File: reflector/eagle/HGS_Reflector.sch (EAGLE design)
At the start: 22 parts, among them J1 U.FL, U1 TQP3M9037, U2 TQP3M903X, U3 LP2985XX-N

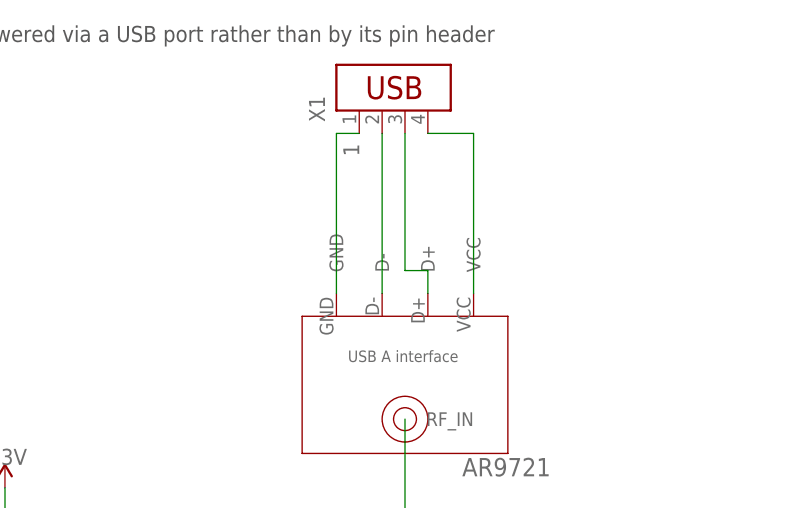
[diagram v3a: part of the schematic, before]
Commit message: Fixed USB pin issue
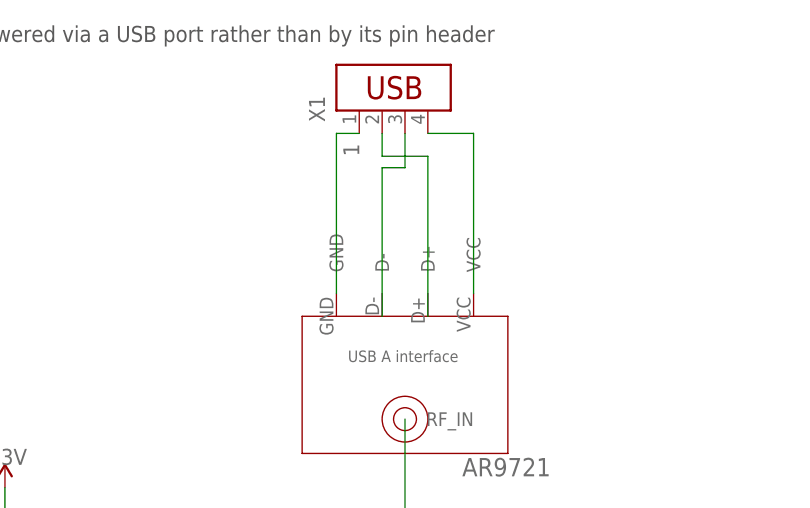
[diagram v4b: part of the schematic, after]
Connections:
- removed net N$16: X1.3
- new net N$6: U$4.D+, X1.2
- net N$14: now also U$4.D-, X1.3; no longer X1.2
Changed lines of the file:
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@@
+</segment>
+</net>
+<net name="N$6" class="0">
+<segment>
+<pinref part="X1" gate="G$1" pin="2"/>
+<wire x1="255.27" y1="189.23" x2="255.27" y2="186.69" width="0.1524" layer="91"/>
+<wire x1="255.27" y1="186.69" x2="260.35" y2="186.69" width="0.1524" layer="91"/>
+<pinref part="U$4" gate="G$1" pin="D+"/>
+<wire x1="260.35" y1="186.69" x2="260.35" y2="168.91" width="0.1524" layer="91"/>
 </segment>
 </net>
 <net name="N$14" class="0">
 <segment>
-<pinref part="X1" gate="G$1" pin="2"/>
-<wire x1="255.27" y1="189.23" x2="255.27" y2="171.45" width="0.1524" layer="91"/>
+<pinref part="U$4" gate="G$1" pin="D-"/>
+<wire x1="255.27" y1="168.91" x2="255.27" y2="185.42" width="0.1524" layer="91"/>
+<wire x1="255.27" y1="185.42" x2="257.81" y2="185.42" width="0.1524" layer="91"/>
+<pinref part="X1" gate="G$1" pin="3"/>
+<wire x1="257.81" y1="185.42" x2="257.81" y2="189.23" width="0.1524" layer="91"/>
 </segment>
 </net>
-<net name="N$16" class="0">
-<segment>
-<pinref part="X1" gate="G$1" pin="3"/>
-<wire x1="257.81" y1="189.23" x2="257.81" y2="173.99" width="0.1524" layer="91"/>
-<wire x1="257.81" y1="173.99" x2="260.35" y2="173.99" width="0.1524" layer="91"/>
-<wire x1="260.35" y1="173.99" x2="260.35" y2="171.45" width="0.1524" layer="91"/>
-</segment>
-</net>

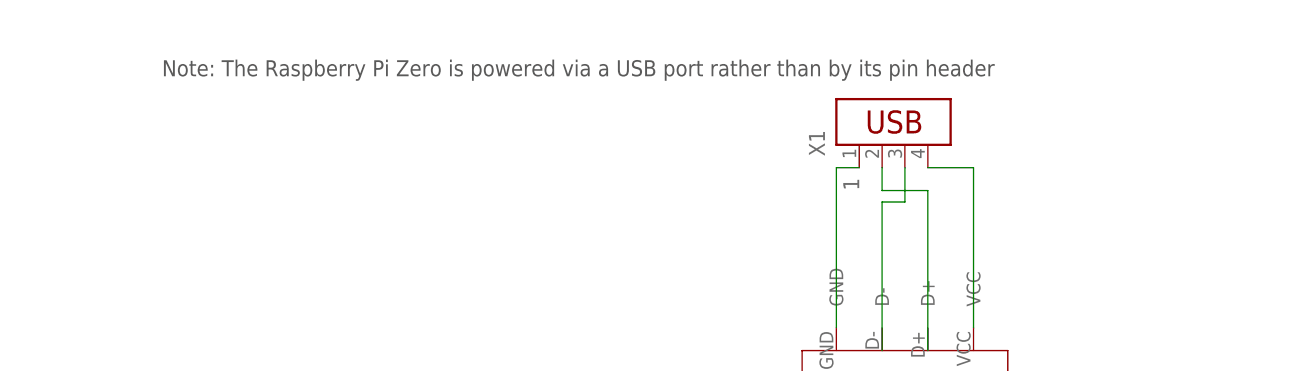
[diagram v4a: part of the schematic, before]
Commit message: Fixed USB A port name
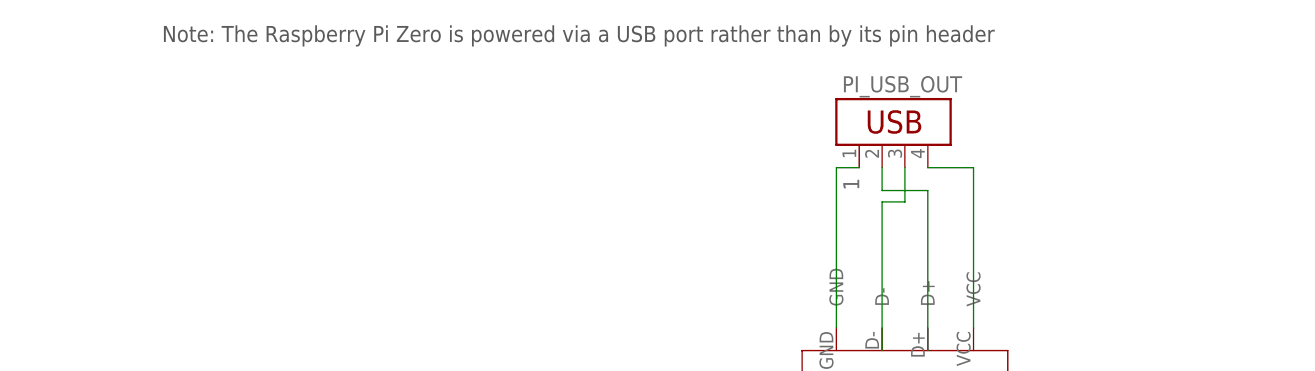
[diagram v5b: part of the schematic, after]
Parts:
- renumbered X1 to PI_USB_OUT
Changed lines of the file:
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@@
 <part name="U$3" library="HGS_Data_Parts" deviceset="1/4_WAVE_TRF" device=""/>
 <part name="ANT1" library="discrete" library_urn="urn:adsk.eagle:library:211" deviceset="ANTENNA" device="" package3d_urn="urn:adsk.eagle:package:12928/1"/>
-<part name="X1" library="con-amp" library_urn="urn:adsk.eagle:library:127" deviceset="USB-787616" device="" package3d_urn="urn:adsk.eagle:package:8081650/1"/>
+<part name="PI_USB_OUT" library="con-amp" library_urn="urn:adsk.eagle:library:127" deviceset="USB-787616" device="" package3d_urn="urn:adsk.eagle:package:8081650/1"/>
 <part name="LED1" library="eagle-ltspice" library_urn="urn:adsk.eagle:library:217" deviceset="LED_E" device="" package3d_urn="urn:adsk.eagle:package:13319/2"/>
 <part name="GND10" library="supply1" library_urn="urn:adsk.eagle:library:371" deviceset="GND" device=""/>
@@
 <text x="180.34" y="27.94" size="3.048" layer="94">OreSat Live Handheld Ground Station Reflector</text>
 <text x="265.43" y="6.35" size="3.048" layer="94">2</text>
-<text x="175.26" y="199.39" size="1.778" layer="97">Note: The Raspberry Pi Zero is powered via a USB port rather than by its pin header</text>
+<text x="175.26" y="203.2" size="1.778" layer="97">Note: The Raspberry Pi Zero is powered via a USB port rather than by its pin header</text>
 <text x="274.32" y="90.17" size="1.778" layer="97" rot="R180">Note: J1 connects to the Atheros WiFi Adapter via coax</text>
 </plain>
@@
 <attribute name="VALUE" x="49.53" y="113.03" size="1.778" layer="96"/>
 </instance>
-<instance part="X1" gate="G$1" x="257.81" y="194.31" smashed="yes" rot="R90">
-<attribute name="NAME" x="248.92" y="190.5" size="1.778" layer="95" rot="R90"/>
+<instance part="PI_USB_OUT" gate="G$1" x="257.81" y="194.31" smashed="yes" rot="R90">
+<attribute name="NAME" x="264.16" y="199.39" size="1.778" layer="95" rot="R180"/>
 <attribute name="VALUE" x="265.43" y="190.5" size="1.778" layer="96" rot="R90"/>
 </instance>
@@
 <net name="1" class="0">
 <segment>
-<pinref part="X1" gate="G$1" pin="1"/>
+<pinref part="PI_USB_OUT" gate="G$1" pin="1"/>
 <label x="252.73" y="186.69" size="1.778" layer="95" rot="R90"/>
 <wire x1="252.73" y1="189.23" x2="250.19" y2="189.23" width="0.1524" layer="91"/>
@@
 <net name="N$15" class="0">
 <segment>
-<pinref part="X1" gate="G$1" pin="4"/>
+<pinref part="PI_USB_OUT" gate="G$1" pin="4"/>
 <wire x1="260.35" y1="189.23" x2="265.43" y2="189.23" width="0.1524" layer="91"/>
 <wire x1="265.43" y1="189.23" x2="265.43" y2="171.45" width="0.1524" layer="91"/>
@@
 <net name="N$6" class="0">
 <segment>
-<pinref part="X1" gate="G$1" pin="2"/>
+<pinref part="PI_USB_OUT" gate="G$1" pin="2"/>
 <wire x1="255.27" y1="189.23" x2="255.27" y2="186.69" width="0.1524" layer="91"/>
 <wire x1="255.27" y1="186.69" x2="260.35" y2="186.69" width="0.1524" layer="91"/>
@@
 <wire x1="255.27" y1="168.91" x2="255.27" y2="185.42" width="0.1524" layer="91"/>
 <wire x1="255.27" y1="185.42" x2="257.81" y2="185.42" width="0.1524" layer="91"/>
-<pinref part="X1" gate="G$1" pin="3"/>
+<pinref part="PI_USB_OUT" gate="G$1" pin="3"/>
 <wire x1="257.81" y1="185.42" x2="257.81" y2="189.23" width="0.1524" layer="91"/>
 </segment>

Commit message: Schematic, board and BOM updates
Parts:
- removed C5, C7: (no value), oresat-rcl:C-EU0402-C-NOSILK
- removed U1: TQP3M9037, U-Qorvo-TQP3M9037-LNA:TQP3M9037
- removed U2: TQP3M903X, U-Qorvo-TQP3M903x-LNA:TQP3M903X
- added C11: 100 pF, oresat-rcl:C-EU0603-C-NOSILK
- added C12: 1 uF, oresat-rcl:C-EU0603-C-NOSILK
- added C14: 100 pF, oresat-rcl:C-EU0402-C-NOSILK
- added L2: (no value), rcl:L-EUL3216C
- added PI_USB_OUT1: (no value), con-amp:USB-787616
- added U$6, U$7: LNA-TP3M9037, HGS_Data_Parts:LNA-TP3M9037
- C1, C6: value (none) -> 100 pF
- C2: value (none) -> 1 uF
- C3, C4: value (none) -> 100 pF; device oresat-rcl:C-EU0603-C-NOSILK -> oresat-rcl:C-EU0402-C-NOSILK
- C8: value 0.1 uF -> 10 nF
- C9: value 0.1 uF -> 2.2 uF
- L1: SPICEPREFIX (none) -> 20 nH
- R9: value (none) -> 2K
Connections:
- removed net N$13: C9.1, U3.VOUT
- removed net N$14: PI_USB_OUT.3, U$4.D-
- removed net N$15: PI_USB_OUT.4
- removed net N$7: C5.1, U$1.RF-OUT
- new net N$16: C14.1, L2.1, U$7.OUT
- new net N$18: PI_USB_OUT.2, PI_USB_OUT1.2, U$4.D+
- new net N$19: PI_USB_OUT.3, PI_USB_OUT1.3, U$4.D-
- new net VCC: PI_USB_OUT.4, PI_USB_OUT1.4, U$4.VCC
- net 1: now also PI_USB_OUT1.1, U$4.GND
- net 3.3V: now also C11.1, C12.1, C9.1, L2.2, U3.VOUT; no longer C3.1, C4.1
- net GND: now also C11.2, C12.2, U$6.GND, U$6.SHTDN, U$7.GND, U$7.SHTDN; no longer C3.2, C4.2, U$3.GND_1, U1.GND, U1.SHTDN, U2.GND, U2.SHTDN
- net N$11: now also U$7.IN; no longer U2.IN
- net N$2: now also C4.1, L1.1, U$6.OUT; no longer J1.SIGNAL, U$2.RF-OUT, U$4.RF_IN
- net N$3: now also C4.2; no longer C7.2, U$2.RF_IN
- net N$4: now also C3.1, U$1.RF-OUT; no longer C5.2, U1.IN
- net N$5: now also J1.SIGNAL, U$2.RF-OUT; no longer C7.1, L1.1, U1.OUT
- net N$6: now also C14.2; no longer PI_USB_OUT.2, U$4.D+
- net N$8: now also C3.2, U$6.IN; no longer U$1.RF_IN, U2.OUT
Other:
- moved on the sheet: ANT1, C1, C2, C3, C4, C6, C8, C9, J1, L1, LED1, PI_USB_OUT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

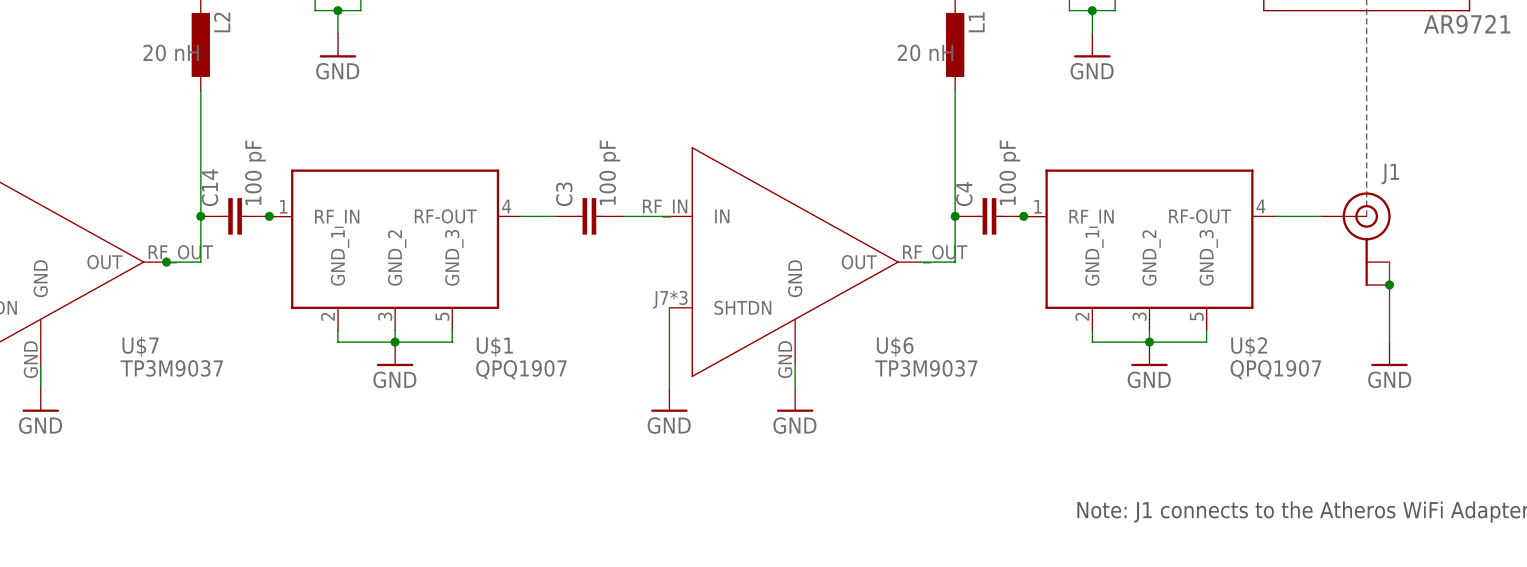
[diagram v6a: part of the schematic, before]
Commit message: Fixed consistency errors by blowing away board and recreating from previous version.
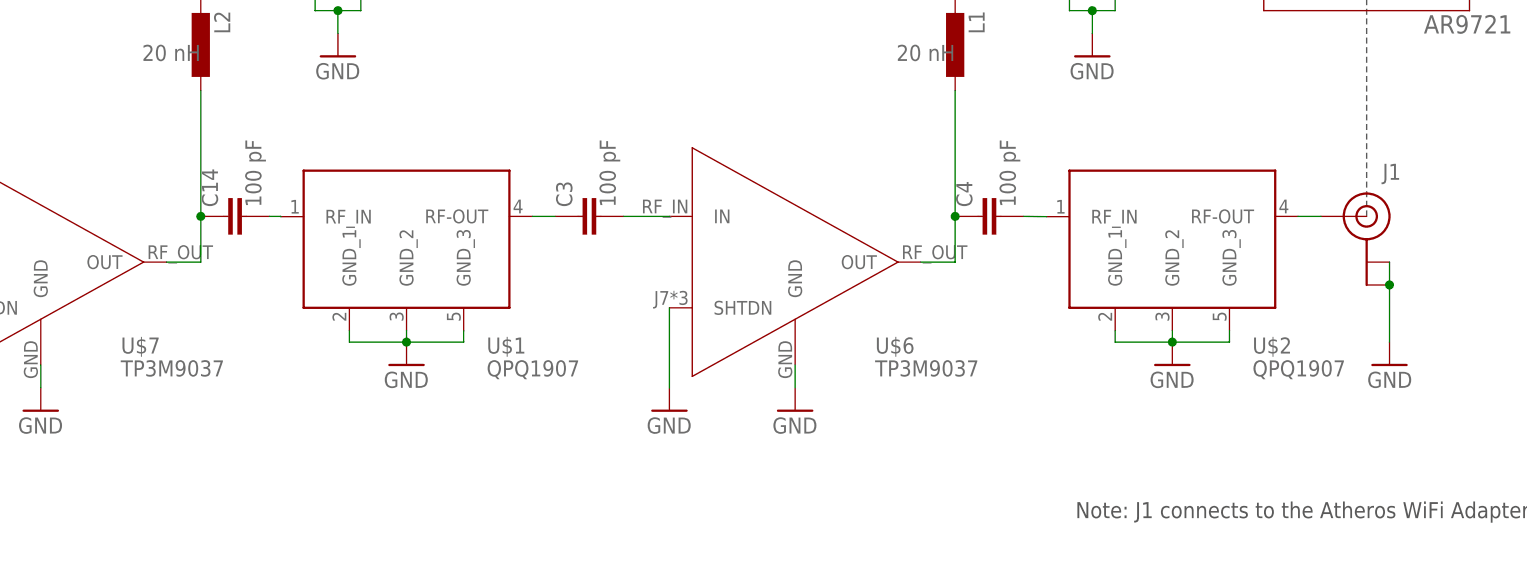
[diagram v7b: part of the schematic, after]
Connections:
- net N$3: now also U$2.RF_IN
- net N$6: now also U$1.RF_IN
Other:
- moved on the sheet: U$1, U$2
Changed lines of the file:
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@@
 <?xml version="1.0" encoding="utf-8"?>
 <!DOCTYPE eagle SYSTEM "eagle.dtd">
-<eagle version="9.4.2">
+<eagle version="9.6.1">
 <drawing>
 <settings>
-<setting alwaysvectorfont="yes"/>
+<setting alwaysvectorfont="no"/>
 <setting verticaltext="up"/>
 </settings>
@@
 <layer number="59" name="tCarbon" color="7" fill="1" visible="no" active="no"/>
 <layer number="60" name="bCarbon" color="7" fill="1" visible="no" active="no"/>
-<layer number="88" name="SimResults" color="9" fill="1" visible="yes" active="yes"/>
-<layer number="89" name="SimProbes" color="9" fill="1" visible="yes" active="yes"/>
+<layer number="88" name="SimResults" color="9" fill="1" visible="no" active="yes"/>
+<layer number="89" name="SimProbes" color="9" fill="1" visible="no" active="yes"/>
 <layer number="90" name="Modules" color="5" fill="1" visible="yes" active="yes"/>
 <layer number="91" name="Nets" color="2" fill="1" visible="yes" active="yes"/>
@@
 <layer number="97" name="Info" color="7" fill="1" visible="yes" active="yes"/>
 <layer number="98" name="Guide" color="6" fill="1" visible="yes" active="yes"/>
-<layer number="99" name="SpiceOrder" color="7" fill="1" visible="yes" active="yes"/>
+<layer number="99" name="SpiceOrder" color="7" fill="1" visible="no" active="yes"/>
 <layer number="100" name="Muster" color="7" fill="1" visible="no" active="no"/>
 <layer number="101" name="Patch_Top" color="12" fill="4" visible="no" active="no"/>
@@
 <attribute name="VALUE" x="79.121" y="114.046" size="1.778" layer="96" rot="R90"/>
 </instance>
-<instance part="GND9" gate="1" x="138.43" y="96.52" smashed="yes">
-<attribute name="VALUE" x="135.89" y="93.98" size="1.778" layer="96"/>
+<instance part="GND9" gate="1" x="139.7" y="96.52" smashed="yes">
+<attribute name="VALUE" x="137.16" y="93.98" size="1.778" layer="96"/>
 </instance>
 <instance part="C8" gate="G$1" x="81.28" y="181.61" smashed="yes" rot="R90">
@@
 <attribute name="VALUE" x="85.09" y="191.77" size="1.778" layer="96" rot="R90"/>
 </instance>
-<instance part="U$1" gate="G$1" x="138.43" y="110.49" smashed="yes">
-<attribute name="NAME" x="147.32" y="97.79" size="1.778" layer="95"/>
+<instance part="U$1" gate="G$1" x="139.7" y="110.49" smashed="yes">
+<attribute name="NAME" x="148.59" y="97.79" size="1.778" layer="95"/>
 </instance>
 <instance part="GND15" gate="1" x="85.09" y="91.44" smashed="yes">
@@
 <attribute name="NAME" x="191.77" y="97.79" size="1.778" layer="95"/>
 </instance>
-<instance part="GND4" gate="1" x="222.25" y="96.52" smashed="yes">
-<attribute name="VALUE" x="219.71" y="93.98" size="1.778" layer="96"/>
-</instance>
-<instance part="U$2" gate="G$1" x="222.25" y="110.49" smashed="yes">
-<attribute name="NAME" x="231.14" y="97.79" size="1.778" layer="95"/>
+<instance part="GND4" gate="1" x="224.79" y="96.52" smashed="yes">
+<attribute name="VALUE" x="222.25" y="93.98" size="1.778" layer="96"/>
+</instance>
+<instance part="U$2" gate="G$1" x="224.79" y="110.49" smashed="yes">
+<attribute name="NAME" x="233.68" y="97.79" size="1.778" layer="95"/>
 </instance>
 <instance part="GND7" gate="1" x="215.9" y="130.81" smashed="yes">
@@
 </segment>
 <segment>
-<wire x1="132.08" y1="99.06" x2="138.43" y2="99.06" width="0.1524" layer="91"/>
-<wire x1="138.43" y1="99.06" x2="144.78" y2="99.06" width="0.1524" layer="91"/>
+<wire x1="133.35" y1="99.06" x2="139.7" y2="99.06" width="0.1524" layer="91"/>
+<wire x1="139.7" y1="99.06" x2="146.05" y2="99.06" width="0.1524" layer="91"/>
 <pinref part="GND9" gate="1" pin="GND"/>
-<junction x="138.43" y="99.06"/>
-<wire x1="132.08" y1="100.33" x2="132.08" y2="99.06" width="0.1524" layer="91"/>
-<wire x1="144.78" y1="99.06" x2="144.78" y2="100.33" width="0.1524" layer="91"/>
-<wire x1="138.43" y1="100.33" x2="138.43" y2="99.06" width="0.1524" layer="91"/>
+<junction x="139.7" y="99.06"/>
+<wire x1="133.35" y1="100.33" x2="133.35" y2="99.06" width="0.1524" layer="91"/>
+<wire x1="146.05" y1="99.06" x2="146.05" y2="100.33" width="0.1524" layer="91"/>
+<wire x1="139.7" y1="100.33" x2="139.7" y2="99.06" width="0.1524" layer="91"/>
 <pinref part="U$1" gate="G$1" pin="GND_3"/>
 <pinref part="U$1" gate="G$1" pin="GND_1"/>
@@
 </segment>
 <segment>
-<wire x1="215.9" y1="99.06" x2="222.25" y2="99.06" width="0.1524" layer="91"/>
-<wire x1="222.25" y1="99.06" x2="228.6" y2="99.06" width="0.1524" layer="91"/>
+<wire x1="218.44" y1="99.06" x2="224.79" y2="99.06" width="0.1524" layer="91"/>
+<wire x1="224.79" y1="99.06" x2="231.14" y2="99.06" width="0.1524" layer="91"/>
 <pinref part="GND4" gate="1" pin="GND"/>
-<junction x="222.25" y="99.06"/>
-<wire x1="215.9" y1="100.33" x2="215.9" y2="99.06" width="0.1524" layer="91"/>
-<wire x1="228.6" y1="99.06" x2="228.6" y2="100.33" width="0.1524" layer="91"/>
-<wire x1="222.25" y1="100.33" x2="222.25" y2="99.06" width="0.1524" layer="91"/>
+<junction x="224.79" y="99.06"/>
+<wire x1="218.44" y1="100.33" x2="218.44" y2="99.06" width="0.1524" layer="91"/>
+<wire x1="231.14" y1="99.06" x2="231.14" y2="100.33" width="0.1524" layer="91"/>
+<wire x1="224.79" y1="100.33" x2="224.79" y2="99.06" width="0.1524" layer="91"/>
 <pinref part="U$2" gate="G$1" pin="GND_3"/>
 <pinref part="U$2" gate="G$1" pin="GND_1"/>
@@
 <pinref part="L2" gate="G$1" pin="1"/>
 <wire x1="116.84" y1="127" x2="116.84" y2="113.03" width="0.1524" layer="91"/>
-<wire x1="116.84" y1="113.03" x2="116.84" y2="107.95" width="0.1524" layer="91"/>
-<wire x1="113.03" y1="107.92" x2="113.03" y2="107.95" width="0.1524" layer="91"/>
-<pinref part="U$7" gate="G$1" pin="OUT"/>
-<wire x1="116.84" y1="107.95" x2="113.03" y2="107.95" width="0.1524" layer="91"/>
-<junction x="113.03" y="107.95"/>
 <pinref part="C14" gate="CE" pin="1"/>
 <junction x="116.84" y="113.03"/>
+<pinref part="U$7" gate="G$1" pin="OUT"/>
+<wire x1="113.03" y1="107.95" x2="116.84" y2="107.95" width="0.1524" layer="91"/>
+<wire x1="116.84" y1="107.95" x2="116.84" y2="113.03" width="0.1524" layer="91"/>
 </segment>
 </net>
@@
 </segment>
 </net>
-<net name="N$6" class="0">
-<segment>
-<pinref part="C14" gate="CE" pin="2"/>
-<junction x="124.46" y="113.03"/>
-</segment>
-</net>
 <net name="N$4" class="0">
 <segment>
 <pinref part="C3" gate="CE" pin="1"/>
 <pinref part="U$1" gate="G$1" pin="RF-OUT"/>
-<wire x1="156.21" y1="113.03" x2="152.4" y2="113.03" width="0.1524" layer="91"/>
+<wire x1="156.21" y1="113.03" x2="153.67" y2="113.03" width="0.1524" layer="91"/>
 </segment>
 </net>
@@
 </segment>
 </net>
-<net name="N$3" class="0">
-<segment>
-<pinref part="C4" gate="CE" pin="2"/>
-<junction x="208.28" y="113.03"/>
-</segment>
-</net>
 <net name="N$5" class="0">
 <segment>
 <pinref part="J1" gate="G$1" pin="SIGNAL"/>
 <pinref part="U$2" gate="G$1" pin="RF-OUT"/>
-<wire x1="241.3" y1="113.03" x2="236.22" y2="113.03" width="0.1524" layer="91"/>
+<wire x1="241.3" y1="113.03" x2="238.76" y2="113.03" width="0.1524" layer="91"/>
 </segment>
 </net>
@@
 </segment>
 </net>
+<net name="N$3" class="0">
+<segment>
+<pinref part="C4" gate="CE" pin="2"/>
+<pinref part="U$2" gate="G$1" pin="RF_IN"/>
+<wire x1="208.28" y1="113.03" x2="210.82" y2="113" width="0.1524" layer="91"/>
+</segment>
+</net>
+<net name="N$6" class="0">
+<segment>
+<pinref part="C14" gate="CE" pin="2"/>
+<pinref part="U$1" gate="G$1" pin="RF_IN"/>
+<wire x1="124.46" y1="113.03" x2="125.73" y2="113.03" width="0.1524" layer="91"/>
+<wire x1="125.73" y1="113.03" x2="125.73" y2="113" width="0.1524" layer="91"/>
+</segment>
+</net>
